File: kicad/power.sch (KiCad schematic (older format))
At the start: 15 parts, among them CON23 PWR_ON, CON24 CON6, Q7 FDC6401N

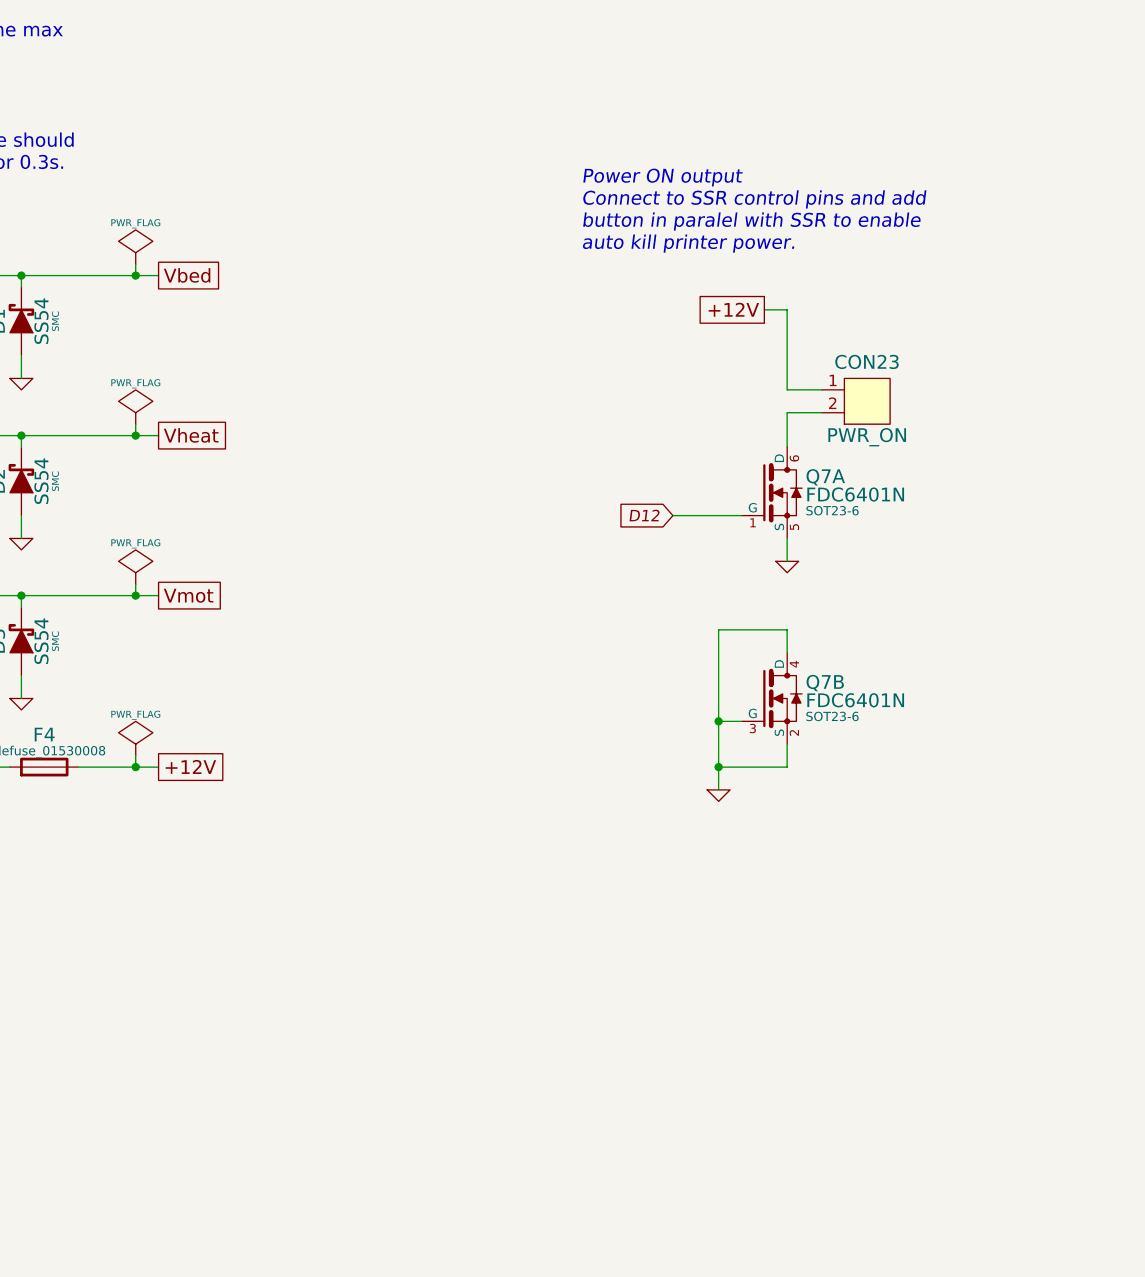
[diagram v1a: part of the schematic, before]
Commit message: Added fan connectors for electronics and power supply
close #15
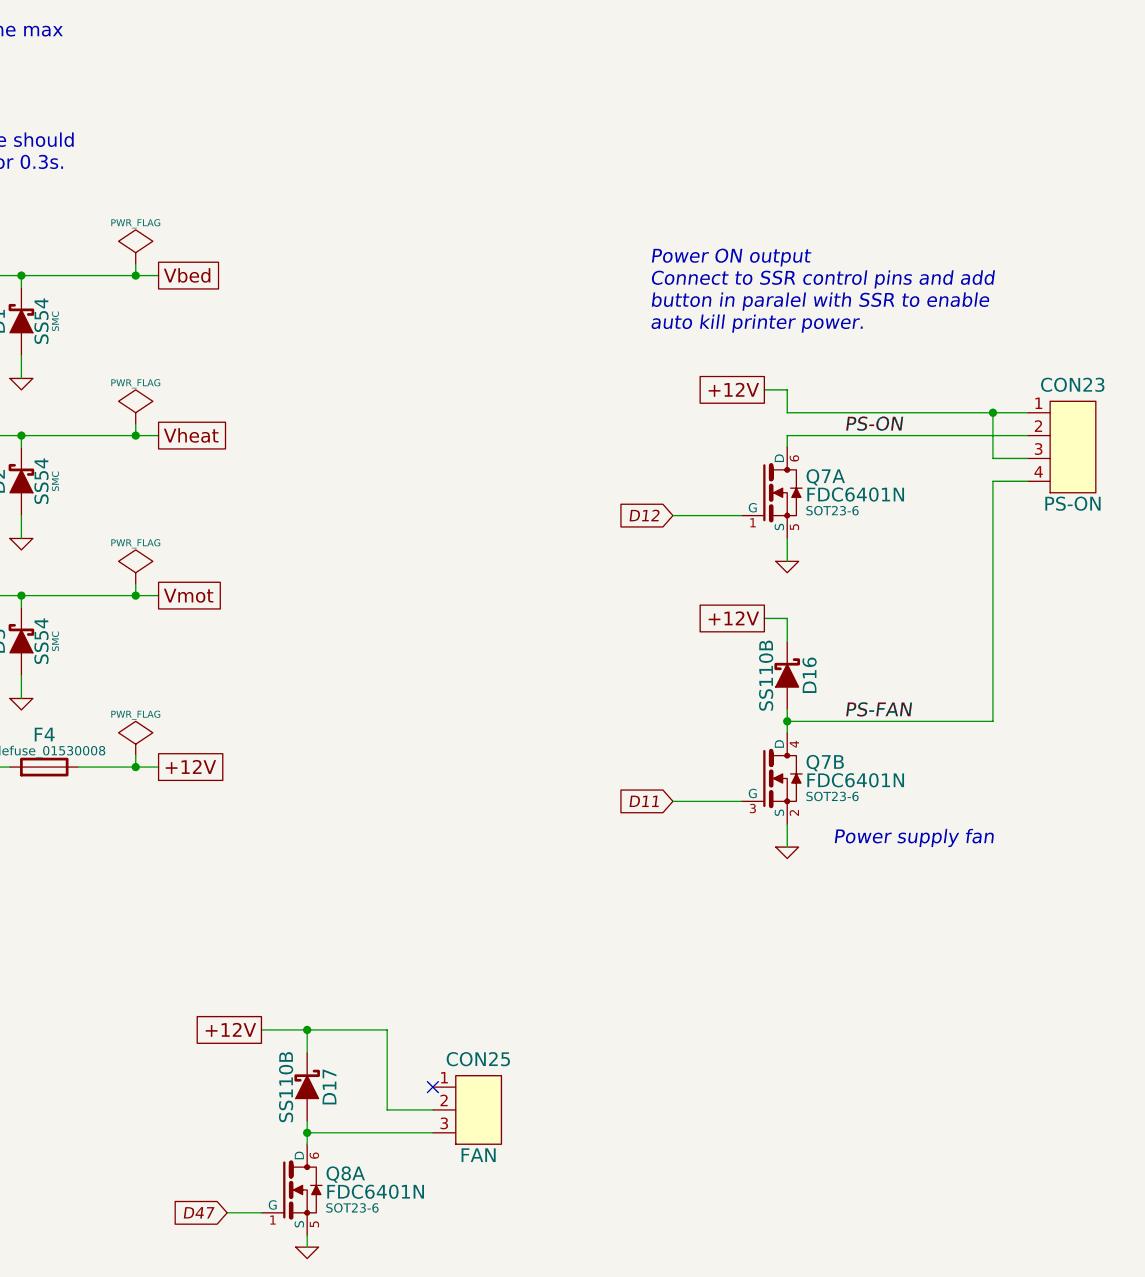
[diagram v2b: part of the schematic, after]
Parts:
- removed CON23: PWR_ON, symbol CON2
- added CON23: PS-ON, symbol CON4
- added CON25: FAN, symbol CON3
- added D16, D17: SS110B, symbol SS110B
- added Q8: FDC6401N, SOT23-6, symbol FDC6401N
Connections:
- net +12V: now also CON23.1, CON23.3, CON25.2, D16.1, D17.1
- net GND: now also Q8.5 (S); no longer Q7.3 (G), Q7.4 (D)
- net PS-ON: now reaches Q7.6 (D)
- net PS-ON: now also CON23.2
- new net: CON25.3, D17.2, Q8.6 (D)
- new net D11: Q7.3 (G)
- new net D47: Q8.1 (G)
- new net PS-FAN: CON23.4, D16.2, Q7.4 (D)
- no-connect marks 0 -> 1
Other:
- note added: "Power supply fan"
- moved on the sheet: Q7B
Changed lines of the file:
@@
 $EndDescr
 $Comp
-L GND #PWR58
+L GND #PWR056
 U 1 1 53943822
 P 1400 3250
-F 0 "#PWR58" H 1400 3250 30  0001 C CNN
+F 0 "#PWR056" H 1400 3250 30  0001 C CNN
 F 1 "GND" H 1400 3180 30  0001 C CNN
 F 2 "" H 1400 3250 60  0000 C CNN
@@
 Littelfuse MINI Blade Fuse\nmodel 0297015 (15A)\n% of rating | opening time max\n135%       | 600s\n200%       | 5 s \n350%       | 0.25 s \n600%       | 0.1 s\nReverse protection diode should \nwithstand at least 50A for 0.3s.
 $Comp
-L GND #PWR60
+L GND #PWR057
 U 1 1 53943829
 P 2900 3250
-F 0 "#PWR60" H 2900 3250 30  0001 C CNN
+F 0 "#PWR057" H 2900 3250 30  0001 C CNN
 F 1 "GND" H 2900 3180 30  0001 C CNN
 F 2 "" H 2900 3250 60  0000 C CNN
@@
 $EndComp
 $Comp
-L GND #PWR57
+L GND #PWR058
 U 1 1 5394382F
 P 2900 2550
-F 0 "#PWR57" H 2900 2550 30  0001 C CNN
+F 0 "#PWR058" H 2900 2550 30  0001 C CNN
 F 1 "GND" H 2900 2480 30  0001 C CNN
 F 2 "" H 2900 2550 60  0000 C CNN
@@
 $EndComp
 $Comp
-L GND #PWR63
+L GND #PWR059
 U 1 1 53943835
 P 2900 3950
-F 0 "#PWR63" H 2900 3950 30  0001 C CNN
+F 0 "#PWR059" H 2900 3950 30  0001 C CNN
 F 1 "GND" H 2900 3880 30  0001 C CNN
 F 2 "" H 2900 3950 60  0000 C CNN
@@
 $EndComp
 $Comp
-L GND #PWR56
+L GND #PWR060
 U 1 1 53943842
 P 1850 2550
-F 0 "#PWR56" H 1850 2550 30  0001 C CNN
+F 0 "#PWR060" H 1850 2550 30  0001 C CNN
 F 1 "GND" H 1850 2480 30  0001 C CNN
 F 2 "" H 1850 2550 60  0000 C CNN
@@
 $EndComp
 $Comp
-L GND #PWR59
+L GND #PWR061
 U 1 1 53943848
 P 1850 3250
-F 0 "#PWR59" H 1850 3250 30  0001 C CNN
+F 0 "#PWR061" H 1850 3250 30  0001 C CNN
 F 1 "GND" H 1850 3180 30  0001 C CNN
 F 2 "" H 1850 3250 60  0000 C CNN
@@
 $EndComp
 $Comp
-L GND #PWR62
+L GND #PWR062
 U 1 1 5394384E
 P 1850 3950
-F 0 "#PWR62" H 1850 3950 30  0001 C CNN
+F 0 "#PWR062" H 1850 3950 30  0001 C CNN
 F 1 "GND" H 1850 3880 30  0001 C CNN
 F 2 "" H 1850 3950 60  0000 C CNN
@@
 $EndComp
 $Comp
-L PWR_FLAG #FLG1
+L PWR_FLAG #FLG063
 U 1 1 539438AC
 P 3400 2050
-F 0 "#FLG1" H 3400 2145 30  0001 C CNN
+F 0 "#FLG063" H 3400 2145 30  0001 C CNN
 F 1 "PWR_FLAG" H 3400 2230 30  0000 C CNN
 F 2 "" H 3400 2050 60  0000 C CNN
@@
 $EndComp
 $Comp
-L PWR_FLAG #FLG2
+L PWR_FLAG #FLG064
 U 1 1 539438B2
 P 3400 2750
-F 0 "#FLG2" H 3400 2845 30  0001 C CNN
+F 0 "#FLG064" H 3400 2845 30  0001 C CNN
 F 1 "PWR_FLAG" H 3400 2930 30  0000 C CNN
 F 2 "" H 3400 2750 60  0000 C CNN
@@
 $EndComp
 $Comp
-L PWR_FLAG #FLG3
+L PWR_FLAG #FLG065
 U 1 1 539438B8
 P 3400 3450
-F 0 "#FLG3" H 3400 3545 30  0001 C CNN
+F 0 "#FLG065" H 3400 3545 30  0001 C CNN
 F 1 "PWR_FLAG" H 3400 3630 30  0000 C CNN
 F 2 "" H 3400 3450 60  0000 C CNN
@@
 $EndComp
 $Comp
-L PWR_FLAG #FLG6
+L PWR_FLAG #FLG066
 U 1 1 539438BE
 P 3400 4200
-F 0 "#FLG6" H 3400 4295 30  0001 C CNN
+F 0 "#FLG066" H 3400 4295 30  0001 C CNN
 F 1 "PWR_FLAG" H 3400 4380 30  0000 C CNN
 F 2 "" H 3400 4200 60  0000 C CNN
@@
 $EndComp
 $Comp
-L PWR_FLAG #FLG7
+L PWR_FLAG #FLG067
 U 1 1 539438C4
 P 1250 4750
-F 0 "#FLG7" H 1250 4845 30  0001 C CNN
+F 0 "#FLG067" H 1250 4845 30  0001 C CNN
 F 1 "PWR_FLAG" H 1250 4930 30  0000 C CNN
 F 2 "" H 1250 4750 60  0000 C CNN
@@
 $EndComp
 $Comp
-L GND #PWR65
+L GND #PWR068
 U 1 1 539438CA
 P 1250 4850
-F 0 "#PWR65" H 1250 4850 30  0001 C CNN
+F 0 "#PWR068" H 1250 4850 30  0001 C CNN
 F 1 "GND" H 1250 4780 30  0001 C CNN
 F 2 "" H 1250 4850 60  0000 C CNN
@@
 IOREF
 $Comp
-L PWR_FLAG #FLG5
+L PWR_FLAG #FLG069
 U 1 1 53943908
 P 1400 4150
-F 0 "#FLG5" H 1400 4245 30  0001 C CNN
+F 0 "#FLG069" H 1400 4245 30  0001 C CNN
 F 1 "PWR_FLAG" H 1400 4330 30  0000 C CNN
 F 2 "" H 1400 4150 60  0000 C CNN
@@
 $EndComp
 $Comp
-L PWR_FLAG #FLG4
+L PWR_FLAG #FLG070
 U 1 1 5394390F
 P 1100 4150
-F 0 "#FLG4" H 1100 4245 30  0001 C CNN
+F 0 "#FLG070" H 1100 4245 30  0001 C CNN
 F 1 "PWR_FLAG" H 1100 4330 30  0000 C CNN
 F 2 "" H 1100 4150 60  0000 C CNN
@@
 	1    1100 4150
 	-1   0    0    1
-$EndComp
-$Comp
-L CON2 CON23
-U 1 1 53943916
-P 6600 2650
-F 0 "CON23" H 6600 2820 60  0000 C CNN
-F 1 "PWR_ON" H 6600 2500 60  0000 C CNN
-F 2 "" H 6600 2650 40  0000 C CNN
-F 3 "" H 6600 2650 40  0000 C CNN
-	1    6600 2650
-	1    0    0    -1
 $EndComp
 $Comp
@@
 L FDC6401N Q7
 U 2 1 53943924
-P 6150 3950
-F 0 "Q7" H 6330 4020 60  0000 L CNN
-F 1 "FDC6401N" H 6330 3940 60  0000 L CNN
-F 2 "SOT23-6" H 6330 3870 40  0000 L CNN
-F 3 "" H 6150 3900 60  0000 C CNN
-	2    6150 3950
-	1    0    0    -1
-$EndComp
-$Comp
-L GND #PWR64
+P 6150 4300
+F 0 "Q7" H 6330 4370 60  0000 L CNN
+F 1 "FDC6401N" H 6330 4290 60  0000 L CNN
+F 2 "SOT23-6" H 6330 4220 40  0000 L CNN
+F 3 "" H 6150 4250 60  0000 C CNN
+	2    6150 4300
+	1    0    0    -1
+$EndComp
+$Comp
+L GND #PWR071
 U 1 1 53943ED6
-P 5950 4350
-F 0 "#PWR64" H 5950 4350 30  0001 C CNN
-F 1 "GND" H 5950 4280 30  0001 C CNN
-F 2 "" H 5950 4350 60  0000 C CNN
-F 3 "" H 5950 4350 60  0000 C CNN
-	1    5950 4350
-	1    0    0    -1
-$EndComp
-$Comp
-L GND #PWR61
+P 6250 4600
+F 0 "#PWR071" H 6250 4600 30  0001 C CNN
+F 1 "GND" H 6250 4530 30  0001 C CNN
+F 2 "" H 6250 4600 60  0000 C CNN
+F 3 "" H 6250 4600 60  0000 C CNN
+	1    6250 4600
+	1    0    0    -1
+$EndComp
+$Comp
+L GND #PWR072
 U 1 1 53943F43
 P 6250 3350
-F 0 "#PWR61" H 6250 3350 30  0001 C CNN
+F 0 "#PWR072" H 6250 3350 30  0001 C CNN
 F 1 "GND" H 6250 3280 30  0001 C CNN
 F 2 "" H 6250 3350 60  0000 C CNN
@@
 	1    0    0    -1
 $EndComp
-Text GLabel 6150 2250 0    60   UnSpc ~ 0
+Text GLabel 6150 2600 0    60   UnSpc ~ 0
 +12V
 Text GLabel 5750 3150 0    50   Input Italic 0
 D12
 Wire Wire Line
-	6250 2600 6250 2250
-Wire Wire Line
-	6400 2600 6250 2600
-Wire Wire Line
-	6250 2700 6250 2850
-Wire Wire Line
-	6250 2250 6150 2250
-Wire Wire Line
-	6400 2700 6250 2700
+	6250 2700 6250 2600
+Wire Wire Line
+	6250 2700 7300 2700
+Wire Wire Line
+	6250 2800 6250 2850
+Wire Wire Line
+	6250 2600 6150 2600
+Wire Wire Line
+	6250 2800 7300 2800
 Wire Wire Line
 	6050 3150 5750 3150
 Wire Wire Line
 	6250 3350 6250 3250
-Connection ~ 5950 4250
-Connection ~ 5950 4050
-Wire Wire Line
-	6250 3650 5950 3650
-Wire Wire Line
-	6250 3750 6250 3650
-Wire Wire Line
-	5950 4050 6050 4050
-Wire Wire Line
-	5950 3650 5950 4350
-Wire Wire Line
-	6250 4250 5950 4250
-Wire Wire Line
-	6250 4150 6250 4250
+Wire Wire Line
+	6250 4000 6250 4100
+Wire Wire Line
+	6250 4500 6250 4600
 Wire Wire Line
 	1100 4150 1100 4050
@@
 Wire Wire Line
 	1400 3100 1350 3100
-Text Notes 5350 2000 0    60   Italic 0
+Text Notes 5650 2350 0    60   Italic 0
 Power ON output\nConnect to SSR control pins and add\nbutton in paralel with SSR to enable \nauto kill printer power.
+$Comp
+L CON4 CON23
+U 1 1 53947AC8
+P 7500 2850
+F 0 "CON23" H 7500 3120 60  0000 C CNN
+F 1 "PS-ON" H 7500 2600 60  0000 C CNN
+F 2 "" H 7500 2850 40  0000 C CNN
+F 3 "" H 7500 2850 40  0000 C CNN
+	1    7500 2850
+	1    0    0    -1
+$EndComp
+Wire Wire Line
+	7300 2900 7150 2900
+Wire Wire Line
+	7150 2900 7150 2700
+Connection ~ 7150 2700
+$Comp
+L SS110B D16
+U 1 1 53948052
+P 6250 3850
+F 0 "D16" H 6250 3750 60  0000 C CNN
+F 1 "SS110B" H 6250 3940 60  0000 C CNN
+F 2 "" V 6100 3812 30  0000 C CNN
+F 3 "" V 6250 3850 60  0000 C CNN
+	1    6250 3850
+	0    -1   -1   0
+$EndComp
+Wire Wire Line
+	6250 3700 6250 3600
+Wire Wire Line
+	6250 3600 6150 3600
+Text GLabel 6150 3600 0    60   UnSpc ~ 0
++12V
+Wire Wire Line
+	6250 4050 7150 4050
+Wire Wire Line
+	7150 4050 7150 3000
+Wire Wire Line
+	7150 3000 7300 3000
+Connection ~ 6250 4050
+Wire Wire Line
+	6050 4400 5750 4400
+Text GLabel 5750 4400 0    50   Input Italic 0
+D11
+Text Notes 6450 4600 0    60   Italic 0
+Power supply fan
+Text Label 6500 2800 0    60   Italic 0
+PS-ON
+Text Label 6500 4050 0    60   Italic 0
+PS-FAN
+$Comp
+L FDC6401N Q8
+U 1 1 539488B9
+P 4050 6100
+F 0 "Q8" H 4230 6170 60  0000 L CNN
+F 1 "FDC6401N" H 4230 6090 60  0000 L CNN
+F 2 "SOT23-6" H 4230 6020 40  0000 L CNN
+F 3 "" H 4050 6050 60  0000 C CNN
+	1    4050 6100
+	1    0    0    -1
+$EndComp
+$Comp
+L CON3 CON25
+U 1 1 53948900
+P 4900 5750
+F 0 "CON25" H 4900 5970 60  0000 C CNN
+F 1 "FAN" H 4900 5550 60  0000 C CNN
+F 2 "" H 4900 5750 40  0000 C CNN
+F 3 "" H 4900 5750 40  0000 C CNN
+	1    4900 5750
+	1    0    0    -1
+$EndComp
+$Comp
+L SS110B D17
+U 1 1 539489C2
+P 4150 5650
+F 0 "D17" H 4150 5550 60  0000 C CNN
+F 1 "SS110B" H 4150 5740 60  0000 C CNN
+F 2 "" V 4000 5612 30  0000 C CNN
+F 3 "" V 4150 5650 60  0000 C CNN
+	1    4150 5650
+	0    -1   -1   0
+$EndComp
+Wire Wire Line
+	4150 5800 4150 5900
+Wire Wire Line
+	4150 5850 4700 5850
+Connection ~ 4150 5850
+Wire Wire Line
+	4700 5750 4500 5750
+Wire Wire Line
+	4500 5400 4500 5750
+Wire Wire Line
+	3950 5400 4500 5400
+Wire Wire Line
+	4150 5500 4150 5400
+Connection ~ 4150 5400
+Text GLabel 3950 5400 0    60   UnSpc ~ 0
++12V
+Wire Wire Line
+	4150 6300 4150 6350
+Wire Wire Line
+	3950 6200 3800 6200
+Text GLabel 3800 6200 0    50   Input Italic 0
+D47
+$Comp
+L GND #PWR073
+U 1 1 53948CCE
+P 4150 6350
+F 0 "#PWR073" H 4150 6350 30  0001 C CNN
+F 1 "GND" H 4150 6280 30  0001 C CNN
+F 2 "" H 4150 6350 60  0000 C CNN
+F 3 "" H 4150 6350 60  0000 C CNN
+	1    4150 6350
+	1    0    0    -1
+$EndComp
+NoConn ~ 4700 5650
 $EndSCHEMATC
